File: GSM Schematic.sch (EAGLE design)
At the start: 20 parts, among them J1 5.5x2.1mm Barrel, J2 AVR_SPI_PRG_62X3_LOCK, Q2 16M, U1 ATMEGA328P-PU, U2 LM317MDT-TR

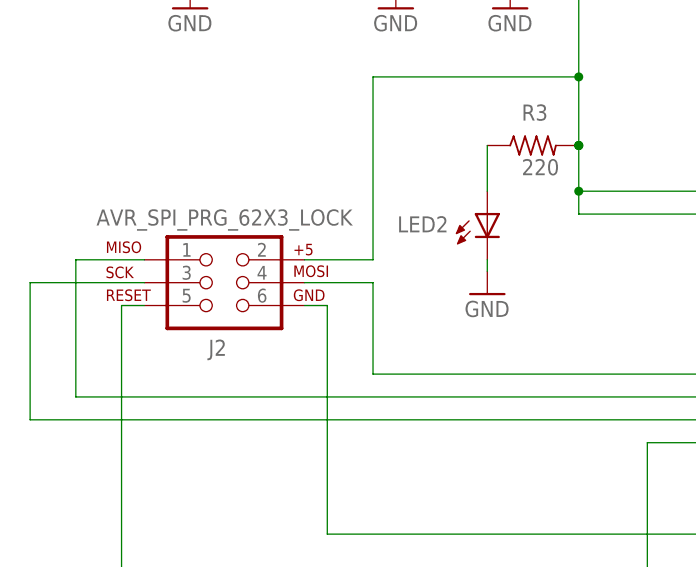
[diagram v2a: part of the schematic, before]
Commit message: Made board and schematic consistent - no ERC erros
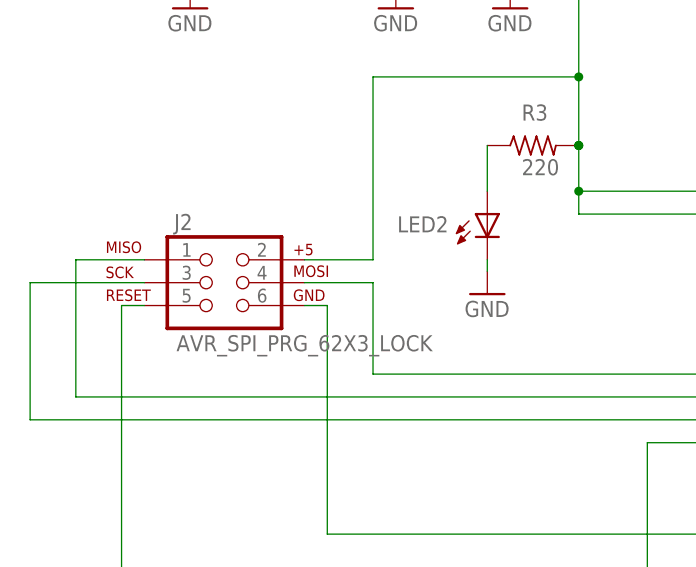
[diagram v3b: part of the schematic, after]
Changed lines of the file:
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@@
 <?xml version="1.0" encoding="utf-8"?>
 <!DOCTYPE eagle SYSTEM "eagle.dtd">
-<eagle version="7.6.0">
+<eagle version="7.7.0">
 <drawing>
 <settings>
@@
 <setting verticaltext="up"/>
 </settings>
-<grid distance="0.05" unitdist="inch" unit="inch" style="lines" multiple="2" display="yes" altdistance="0.01" altunitdist="inch" altunit="inch"/>
+<grid distance="0.1" unitdist="inch" unit="inch" style="lines" multiple="1" display="no" altdistance="0.01" altunitdist="inch" altunit="inch"/>
 <layers>
 <layer number="1" name="Top" color="4" fill="1" visible="no" active="no"/>
@@
 <part name="R1" library="rcl" deviceset="R-US_" device="R0603" value="10k"/>
 <part name="LED2" library="led" deviceset="LED" device="SML0603"/>
-<part name="J2" library="SparkFun-Connectors" deviceset="AVR_SPI_PRG_6" device="2X3_LOCK"/>
 <part name="TX" library="wirepad" deviceset="2,54/0,9" device=""/>
 <part name="RX" library="wirepad" deviceset="2,54/0,9" device=""/>
@@
 <part name="U2" library="MF_IC_Power" deviceset="LM317" device="MDT-TR" value="LM317MDT-TR"/>
 <part name="D1" library="diode" deviceset="1N4004" device=""/>
+<part name="J2" library="SparkFun-Connectors" deviceset="AVR_SPI_PRG_6" device="2X3_LOCK"/>
 </parts>
 <sheets>
@@
 <attribute name="VALUE" x="191.135" y="165.608" size="1.778" layer="96" rot="R90"/>
 </instance>
-<instance part="J2" gate="G$1" x="154.94" y="162.56" smashed="yes">
-<attribute name="NAME" x="154.432" y="154.432" size="1.778" layer="95"/>
-<attribute name="VALUE" x="141.986" y="168.91" size="1.778" layer="96"/>
-</instance>
 <instance part="TX" gate="1" x="264.16" y="167.64" smashed="yes" rot="R180">
 <attribute name="NAME" x="265.303" y="170.8658" size="1.778" layer="95" rot="R180"/>
@@
 <attribute name="VALUE" x="280.67" y="133.5786" size="1.778" layer="96"/>
 </instance>
+<instance part="J2" gate="G$1" x="154.94" y="162.56"/>
 </instances>
 <busses>
@@
 <junction x="218.44" y="134.62"/>
 <wire x1="218.44" y1="134.62" x2="218.44" y2="130.81" width="0.1524" layer="91"/>
-<pinref part="J2" gate="G$1" pin="6"/>
 <wire x1="167.64" y1="134.62" x2="218.44" y2="134.62" width="0.1524" layer="91"/>
 <wire x1="165.1" y1="160.02" x2="167.64" y2="160.02" width="0.1524" layer="91"/>
 <wire x1="167.64" y1="160.02" x2="167.64" y2="134.62" width="0.1524" layer="91"/>
+<pinref part="J2" gate="G$1" pin="6"/>
 </segment>
 <segment>
@@
 <net name="N$7" class="0">
 <segment>
-<pinref part="J2" gate="G$1" pin="4"/>
 <wire x1="165.1" y1="162.56" x2="172.72" y2="162.56" width="0.1524" layer="91"/>
 <wire x1="172.72" y1="162.56" x2="172.72" y2="152.4" width="0.1524" layer="91"/>
 <wire x1="172.72" y1="152.4" x2="218.44" y2="152.4" width="0.1524" layer="91"/>
 <pinref part="U1" gate="A" pin="PB3"/>
+<pinref part="J2" gate="G$1" pin="4"/>
 </segment>
 </net>
@@
 <wire x1="139.7" y1="149.86" x2="218.44" y2="149.86" width="0.1524" layer="91"/>
 <pinref part="U1" gate="A" pin="PB4"/>
-<pinref part="J2" gate="G$1" pin="1"/>
 <wire x1="147.32" y1="165.1" x2="139.7" y2="165.1" width="0.1524" layer="91"/>
 <wire x1="139.7" y1="165.1" x2="139.7" y2="149.86" width="0.1524" layer="91"/>
+<pinref part="J2" gate="G$1" pin="1"/>
 </segment>
 </net>
@@
 <wire x1="173.99" y1="124.46" x2="254" y2="124.46" width="0.1524" layer="91"/>
 <wire x1="254" y1="124.46" x2="254" y2="134.62" width="0.1524" layer="91"/>
-<pinref part="J2" gate="G$1" pin="5"/>
 <wire x1="147.32" y1="160.02" x2="144.78" y2="160.02" width="0.1524" layer="91"/>
 <wire x1="144.78" y1="160.02" x2="144.78" y2="124.46" width="0.1524" layer="91"/>
 <pinref part="R1" gate="G$1" pin="2"/>
 <junction x="173.99" y="124.46"/>
+<pinref part="J2" gate="G$1" pin="5"/>
 </segment>
 </net>
@@
 <junction x="195.58" y="177.8"/>
 <junction x="195.58" y="185.42"/>
-<pinref part="J2" gate="G$1" pin="2"/>
 <wire x1="215.9" y1="170.18" x2="195.58" y2="170.18" width="0.1524" layer="91"/>
 <wire x1="172.72" y1="185.42" x2="195.58" y2="185.42" width="0.1524" layer="91"/>
@@
 <pinref part="U2" gate="G$1" pin="VOUT"/>
 <wire x1="182.88" y1="205.74" x2="187.96" y2="205.74" width="0.1524" layer="91"/>
+<pinref part="J2" gate="G$1" pin="2"/>
 </segment>
 </net>
@@
 <segment>
 <pinref part="U1" gate="A" pin="PB5"/>
-<pinref part="J2" gate="G$1" pin="3"/>
 <wire x1="147.32" y1="162.56" x2="134.62" y2="162.56" width="0.1524" layer="91"/>
 <wire x1="134.62" y1="162.56" x2="134.62" y2="147.32" width="0.1524" layer="91"/>
 <wire x1="218.44" y1="147.32" x2="134.62" y2="147.32" width="0.1524" layer="91"/>
-</segment>
-</net>
+<pinref part="J2" gate="G$1" pin="3"/>
+</segment>
+</net>
